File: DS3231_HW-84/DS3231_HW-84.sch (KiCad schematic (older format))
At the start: 16 parts, among them J1 Conn_01x06, J2 Conn_01x04, U1 DS3231SN, U2 24CS32N

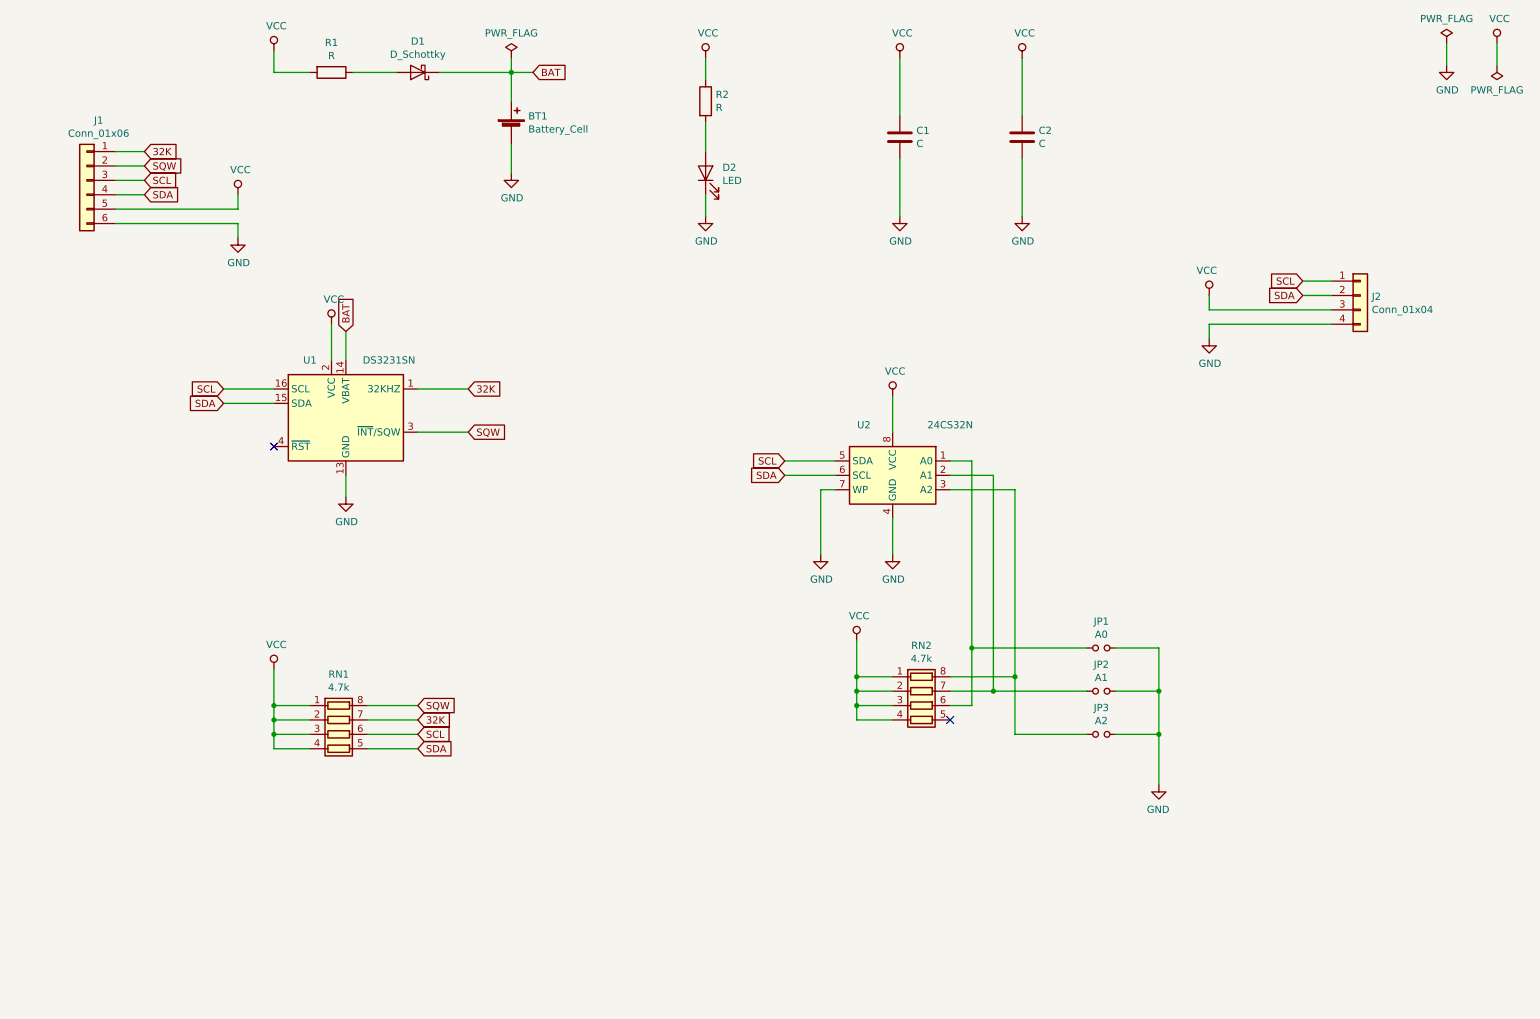
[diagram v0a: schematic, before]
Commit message: DS3231_HW-84 was added
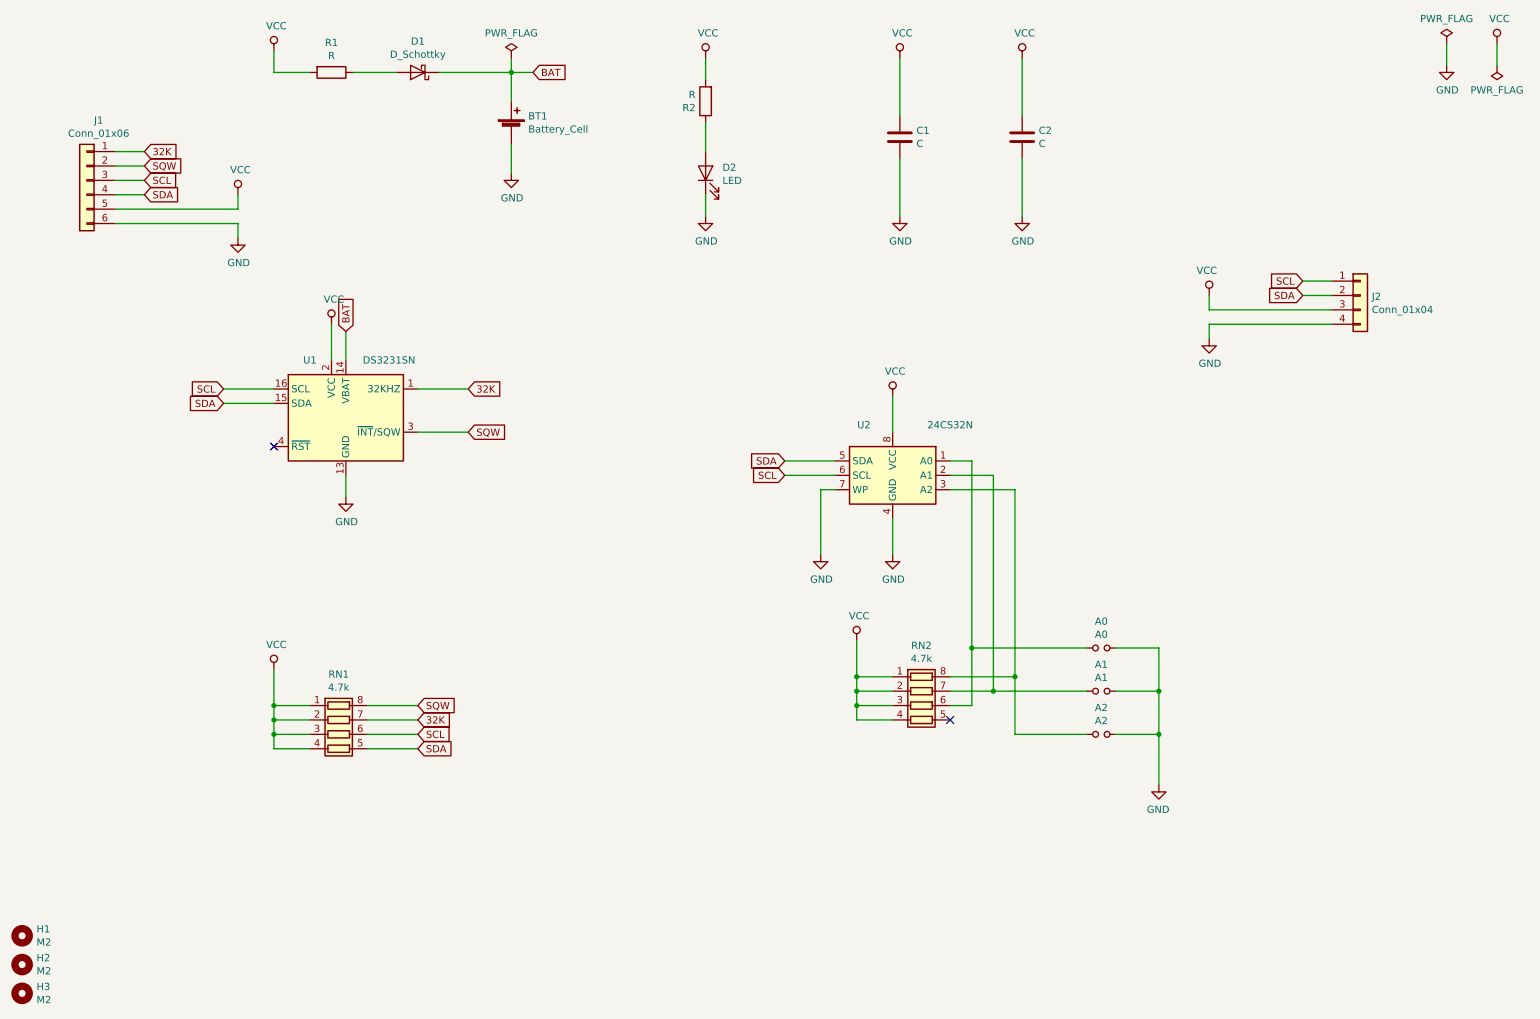
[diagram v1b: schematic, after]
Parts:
- added H1, H2, H3: M2, MountingHole:MountingHole_2.2mm_M2, symbol Mechanical:MountingHole
- BT1: footprint (none) -> BatteryU:CH224-2032LF
- J1: footprint Connector_PinHeader_2.54mm:PinHeader_1x06_P2.54mm_Horizontal -> Connector_PinHeader_2.54mm:PinHeader_1x06_P2.54mm_Vertical
- J2: footprint Connector_PinHeader_2.54mm:PinHeader_1x04_P2.54mm_Horizontal -> Connector_PinHeader_2.54mm:PinHeader_1x04_P2.54mm_Vertical
- renumbered JP1 to A0, JP2 to A1, JP3 to A2
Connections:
- net SCL: now also U2.6 (SCL); no longer U2.5 (SDA)
- net SDA: now also U2.5 (SDA); no longer U2.6 (SCL)
- net VCC: now also R2.2; no longer R2.1
- net at D2.2 (A): now also R2.1; no longer R2.2
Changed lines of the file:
@@
 F 0 "J1" H 1118 2117 50  0000 C CNN
 F 1 "Conn_01x06" H 1118 2026 50  0000 C CNN
-F 2 "Connector_PinHeader_2.54mm:PinHeader_1x06_P2.54mm_Horizontal" H 1200 1700 50  0001 C CNN
+F 2 "Connector_PinHeader_2.54mm:PinHeader_1x06_P2.54mm_Vertical" H 1200 1700 50  0001 C CNN
 F 3 "~" H 1200 1700 50  0001 C CNN
 	1    1200 1700
@@
 F 0 "J2" H 10130 2492 50  0000 L CNN
 F 1 "Conn_01x04" H 10130 2401 50  0000 L CNN
-F 2 "Connector_PinHeader_2.54mm:PinHeader_1x04_P2.54mm_Horizontal" H 10050 2500 50  0001 C CNN
+F 2 "Connector_PinHeader_2.54mm:PinHeader_1x04_P2.54mm_Vertical" H 10050 2500 50  0001 C CNN
 F 3 "~" H 10050 2500 50  0001 C CNN
 	1    10050 2500
@@
 $EndComp
 $Comp
-L Device:Jumper_NO_Small JP1
+L Device:Jumper_NO_Small A0
 U 1 1 605A711D
 P 8250 4950
-F 0 "JP1" H 8250 5135 50  0000 C CNN
+F 0 "A0" H 8250 5135 50  0000 C CNN
 F 1 "A0" H 8250 5044 50  0000 C CNN
 F 2 "Jumper:SolderJumper-2_P1.3mm_Open_Pad1.0x1.5mm" H 8250 4950 50  0001 C CNN
@@
 $EndComp
 $Comp
-L Device:Jumper_NO_Small JP2
+L Device:Jumper_NO_Small A1
 U 1 1 605A8056
 P 8250 5250
-F 0 "JP2" H 8250 5435 50  0000 C CNN
+F 0 "A1" H 8250 5435 50  0000 C CNN
 F 1 "A1" H 8250 5344 50  0000 C CNN
 F 2 "Jumper:SolderJumper-2_P1.3mm_Open_Pad1.0x1.5mm" H 8250 5250 50  0001 C CNN
@@
 $EndComp
 $Comp
-L Device:Jumper_NO_Small JP3
+L Device:Jumper_NO_Small A2
 U 1 1 605A8317
 P 8250 5550
-F 0 "JP3" H 8250 5735 50  0000 C CNN
+F 0 "A2" H 8250 5735 50  0000 C CNN
 F 1 "A2" H 8250 5644 50  0000 C CNN
 F 2 "Jumper:SolderJumper-2_P1.3mm_Open_Pad1.0x1.5mm" H 8250 5550 50  0001 C CNN
@@
 F 0 "BT1" H 4268 1446 50  0000 L CNN
 F 1 "Battery_Cell" H 4268 1355 50  0000 L CNN
-F 2 "" V 4150 1410 50  0001 C CNN
+F 2 "BatteryU:CH224-2032LF" V 4150 1410 50  0001 C CNN
 F 3 "~" V 4150 1410 50  0001 C CNN
 	1    4150 1350
@@
 F 3 "~" H 5500 1150 50  0001 C CNN
 	1    5500 1150
-	1    0    0    -1
+	-1   0    0    1
 $EndComp
 $Comp
@@
 Wire Wire Line
 	2500 3150 2150 3150
+Text GLabel 6050 3650 0    50   Input ~ 0
+SDA
 Text GLabel 6050 3750 0    50   Input ~ 0
-SDA
-Text GLabel 6050 3650 0    50   Input ~ 0
 SCL
 Wire Wire Line
@@
 Wire Wire Line
 	4150 850  4150 950
+$Comp
+L Mechanical:MountingHole H1
+U 1 1 606218C4
+P 750 6950
+F 0 "H1" H 850 6996 50  0000 L CNN
+F 1 "M2" H 850 6905 50  0000 L CNN
+F 2 "MountingHole:MountingHole_2.2mm_M2" H 750 6950 50  0001 C CNN
+F 3 "~" H 750 6950 50  0001 C CNN
+	1    750  6950
+	1    0    0    -1
+$EndComp
+$Comp
+L Mechanical:MountingHole H2
+U 1 1 60621F2A
+P 750 7150
+F 0 "H2" H 850 7196 50  0000 L CNN
+F 1 "M2" H 850 7105 50  0000 L CNN
+F 2 "MountingHole:MountingHole_2.2mm_M2" H 750 7150 50  0001 C CNN
+F 3 "~" H 750 7150 50  0001 C CNN
+	1    750  7150
+	1    0    0    -1
+$EndComp
+$Comp
+L Mechanical:MountingHole H3
+U 1 1 60622452
+P 750 7350
+F 0 "H3" H 850 7396 50  0000 L CNN
+F 1 "M2" H 850 7305 50  0000 L CNN
+F 2 "MountingHole:MountingHole_2.2mm_M2" H 750 7350 50  0001 C CNN
+F 3 "~" H 750 7350 50  0001 C CNN
+	1    750  7350
+	1    0    0    -1
+$EndComp
 $EndSCHEMATC
